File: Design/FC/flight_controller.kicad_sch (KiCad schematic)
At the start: 3 parts, among them U1 STM32H747BIT6

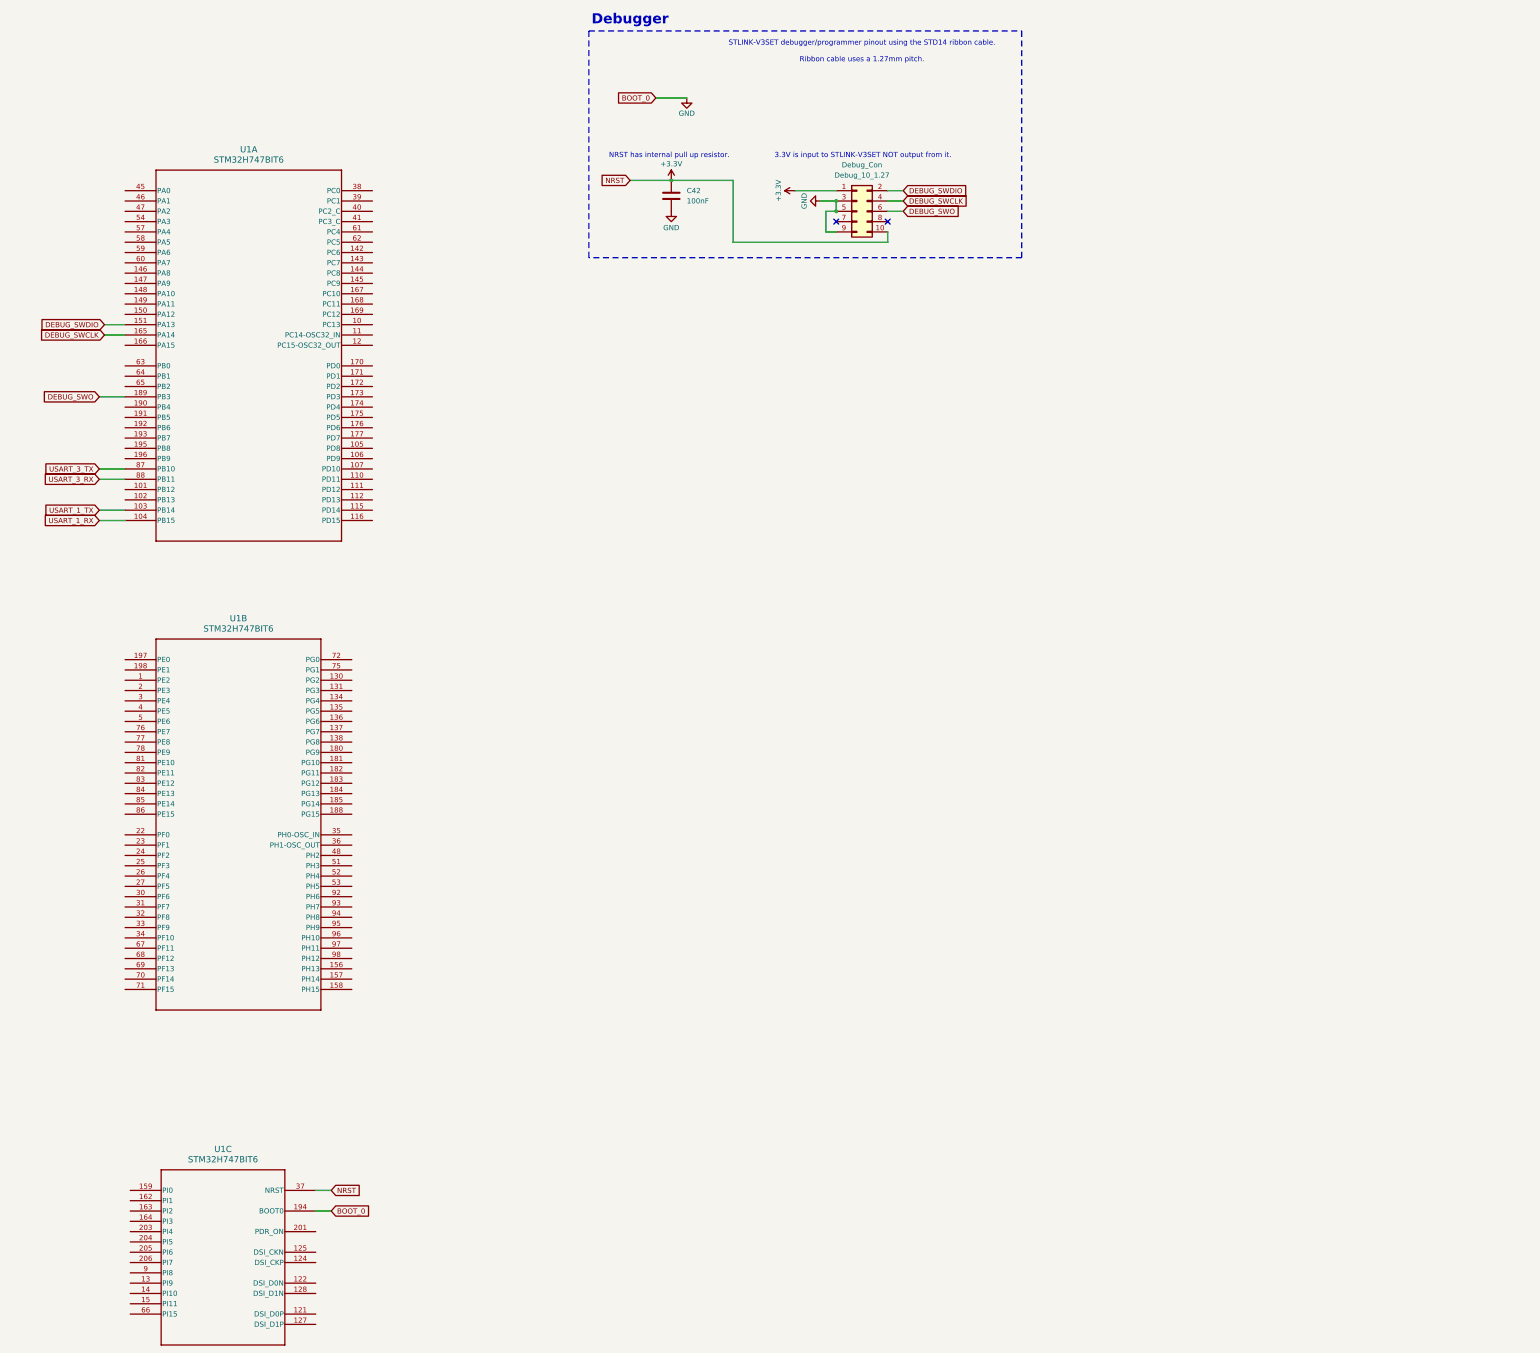
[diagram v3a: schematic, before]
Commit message: started adding periphs
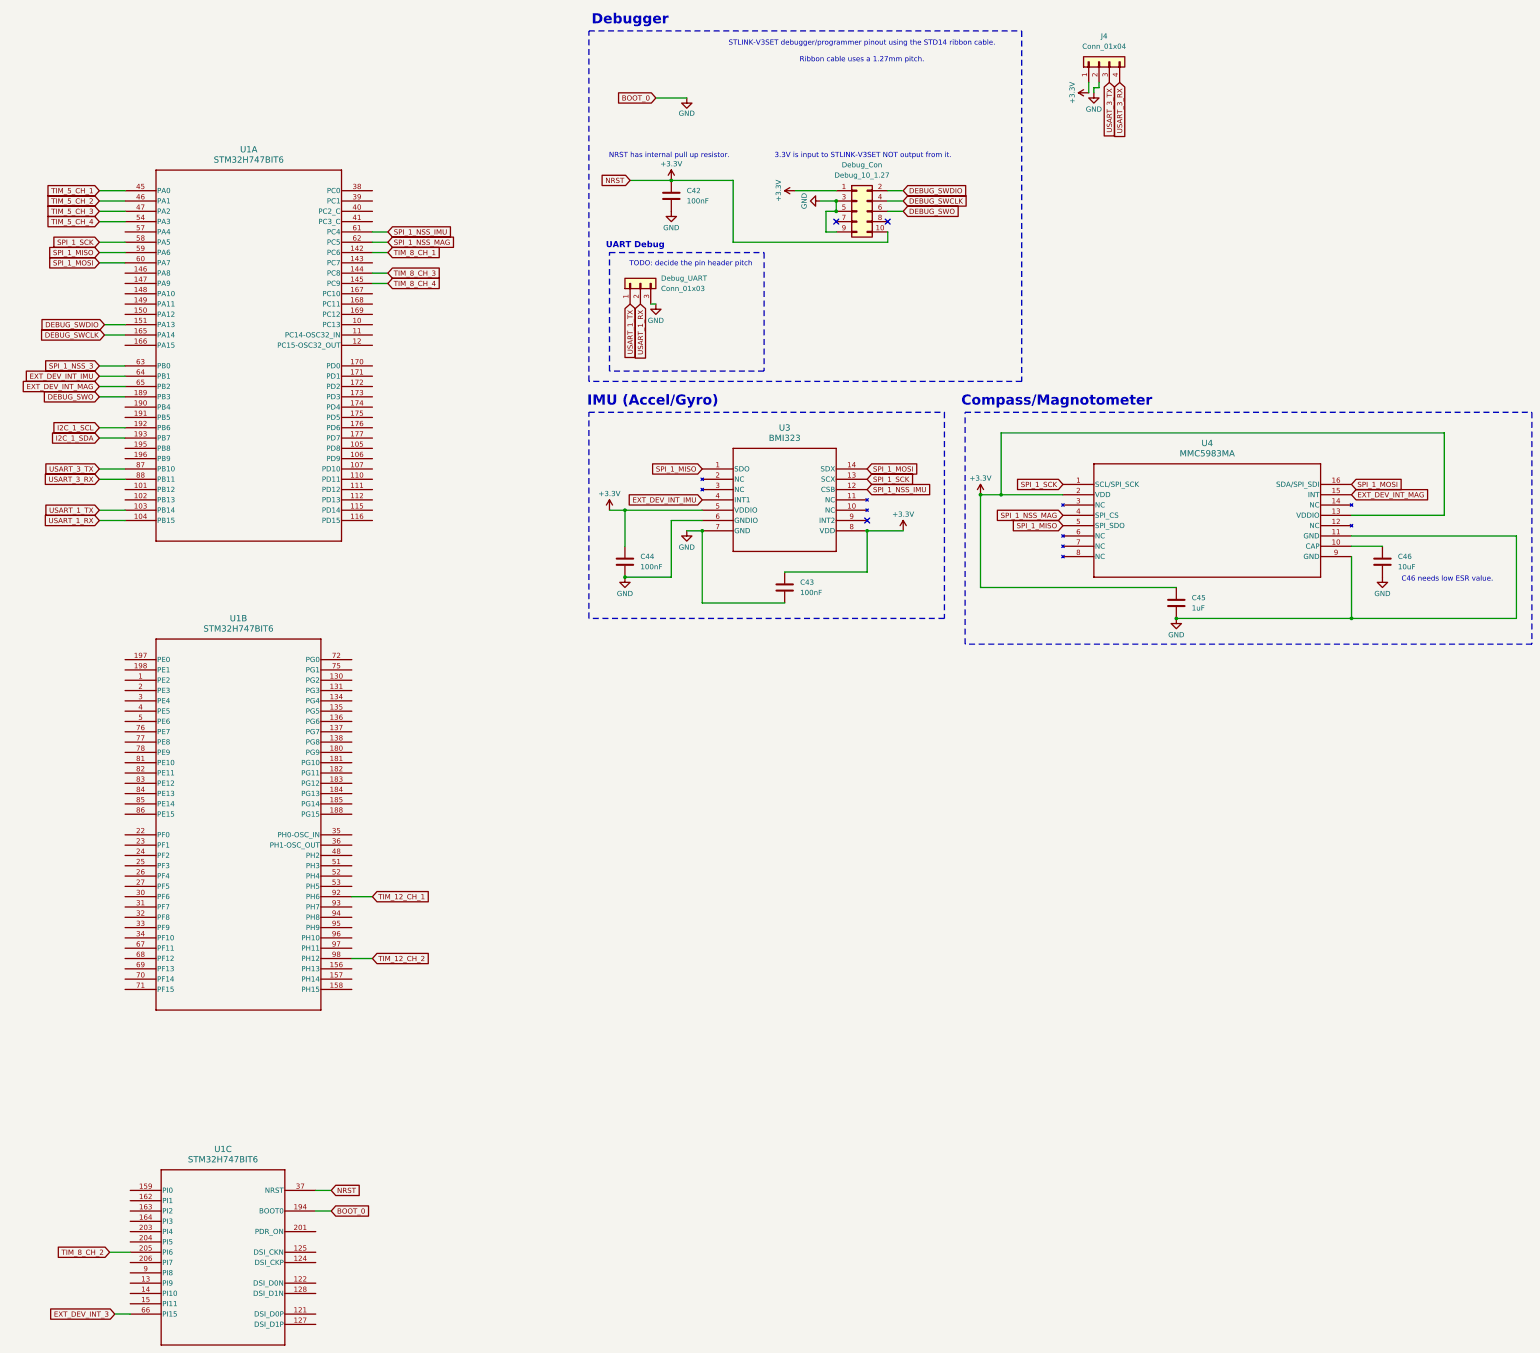
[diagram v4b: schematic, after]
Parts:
- added C43, C44: 100nF, symbol Device:C
- added C45: 1uF, symbol Device:C
- added C46: 10uF, symbol Device:C
- added Debug_UART: Conn_01x03, symbol Connector_Generic:Conn_01x03
- added J4: Conn_01x04, symbol Connector_Generic:Conn_01x04
- added U3: BMI323, BMI323_BOS, symbol BMI323:BMI323
- added U4: MMC5983MA, MMC5983MA_MEM, symbol MMC5983MA:MMC5983MA
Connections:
- net +3.3V: now also C43.1, C44.1, C45.1, J4.1 (Pin_1), U3.5 (VDDIO), U3.8 (VDD), U4.13 (VDDIO), U4.2 (VDD)
- net GND: now also C43.2, C44.2, C45.2, C46.2, Debug_UART.3 (Pin_3), J4.2 (Pin_2), U3.6 (GNDIO), U3.7 (GND), U4.11 (GND), U4.9 (GND)
- net USART_1_RX: now also Debug_UART.2 (Pin_2)
- net USART_1_TX: now also Debug_UART.1 (Pin_1)
- net USART_3_RX: now also J4.4 (Pin_4)
- net USART_3_TX: now also J4.3 (Pin_3)
- net TIM_8_CH_1: now reaches U1.142 (PC6)
- net TIM_8_CH_3: now reaches U1.144 (PC8)
- net TIM_8_CH_4: now reaches U1.145 (PC9)
- net I2C_1_SCL: now reaches U1.192 (PB6)
- net I2C_1_SDA: now reaches U1.193 (PB7)
- net TIM_5_CH_1: now reaches U1.45 (PA0)
- net TIM_5_CH_2: now reaches U1.46 (PA1)
- net TIM_5_CH_3: now reaches U1.47 (PA2)
- net TIM_5_CH_4: now reaches U1.54 (PA3)
- net SPI_1_SCK: now reaches U1.58 (PA5)
- net SPI_1_SCK: now also U3.13 (SCX), U4.1 (SCL/SPI_SCK)
- net SPI_1_MISO: now reaches U1.59 (PA6)
- net SPI_1_MISO: now also U3.1 (SDO), U4.5 (SPI_SDO)
- net SPI_1_MOSI: now reaches U1.60 (PA7)
- net SPI_1_MOSI: now also U3.14 (SDX), U4.16 (SDA/SPI_SDI)
- net SPI_1_NSS_IMU: now reaches U1.61 (PC4)
- net SPI_1_NSS_IMU: now also U3.12 (CSB)
- net SPI_1_NSS_MAG: now reaches U1.62 (PC5)
- net SPI_1_NSS_MAG: now also U4.4 (SPI_CS)
- net SPI_1_NSS_3: now reaches U1.63 (PB0)
- net EXT_DEV_INT_IMU: now reaches U1.64 (PB1)
- net EXT_DEV_INT_IMU: now also U3.4 (INT1)
- net EXT_DEV_INT_MAG: now reaches U1.65 (PB2)
- net EXT_DEV_INT_MAG: now also U4.15 (INT)
- net TIM_8_CH_2: now reaches U1.205 (PI6)
- net EXT_DEV_INT_3: now reaches U1.66 (PI15)
- net TIM_12_CH_1: now reaches U1.92 (PH6)
- net TIM_12_CH_2: now reaches U1.98 (PH12)
- new net: C46.1, U4.10 (CAP)
- no-connect marks 2 -> 3
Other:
- note added: "C46 needs low ESR value."
- note added: "Compass/Magnotometer"
- note added: "IMU (Accel/Gyro)"
- note added: "TODO: decide the pin header pitch"
- note added: "UART Debug"

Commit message: continuing to add periphs
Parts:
- added C47, C48: 100nF, symbol Device:C
- added JL_Servo_2, L_Servo_1, L_Servo_3, L_Servo_4, R_Servo_1, R_Servo_2, R_Servo_3, R_Servo_4: Conn_01x03, symbol Connector_Generic:Conn_01x03
- added L_Motor, R_Motor: Conn_01x02, symbol Connector_Generic:Conn_01x02
- added U5: BMP390, BMP390-10LGA_2X2X0p75_BOS, symbol BMP390:BMP390
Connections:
- net +3.3V: now also C47.1, C48.1, U5.1 (VDDIO), U5.10 (VDD)
- net GND: now also C47.2, C48.2, JL_Servo_2.1 (Pin_1), L_Motor.1 (Pin_1), L_Servo_1.1 (Pin_1), L_Servo_3.1 (Pin_1), L_Servo_4.1 (Pin_1), R_Motor.1 (Pin_1), R_Servo_1.1 (Pin_1), R_Servo_2.1 (Pin_1), R_Servo_3.1 (Pin_1), R_Servo_4.1 (Pin_1), U5.3 (VSS), U5.8 (VSS), U5.9 (VSS)
- net SPI_1_MISO: now also U5.5 (SDO)
- net SPI_1_MOSI: now also U5.4 (SDI)
- net SPI_1_SCK: now also U5.2 (SCK)
- net TIM_5_CH_1: now also L_Servo_1.3 (Pin_3)
- net TIM_5_CH_2: now also JL_Servo_2.3 (Pin_3)
- net TIM_5_CH_3: now also L_Servo_3.3 (Pin_3)
- net TIM_5_CH_4: now also L_Servo_4.3 (Pin_3)
- net TIM_8_CH_1: now also R_Servo_1.3 (Pin_3)
- net TIM_8_CH_2: now also R_Servo_2.3 (Pin_3)
- net TIM_8_CH_3: now also R_Servo_3.3 (Pin_3)
- net TIM_8_CH_4: now also R_Servo_4.3 (Pin_3)
- net TIM_4_CH_1: now reaches U1.111 (PD12)
- net TIM_4_CH_1: now also R_Motor.2 (Pin_2)
- net TIM_16_CH_1: now reaches U1.30 (PF6)
- net TIM_16_CH_1: now also L_Motor.2 (Pin_2)
- net EXT_DEV_INT_3 renamed EXT_DEV_INT_BARO
- net EXT_DEV_INT_BARO: now also U5.7 (INT)
- net SPI_1_NSS_3 renamed SPI_1_NSS_BARO
- net SPI_1_NSS_BARO: now also U5.6 (CSB)
- new net +5V: JL_Servo_2.2 (Pin_2), L_Servo_1.2 (Pin_2), L_Servo_3.2 (Pin_2), L_Servo_4.2 (Pin_2), R_Servo_1.2 (Pin_2), R_Servo_2.2 (Pin_2), R_Servo_3.2 (Pin_2), R_Servo_4.2 (Pin_2)
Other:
- note added: "Barometer"
- note added: "Servo (GND, VCC, Signal) and Motor (GND, Signal) Connectors"

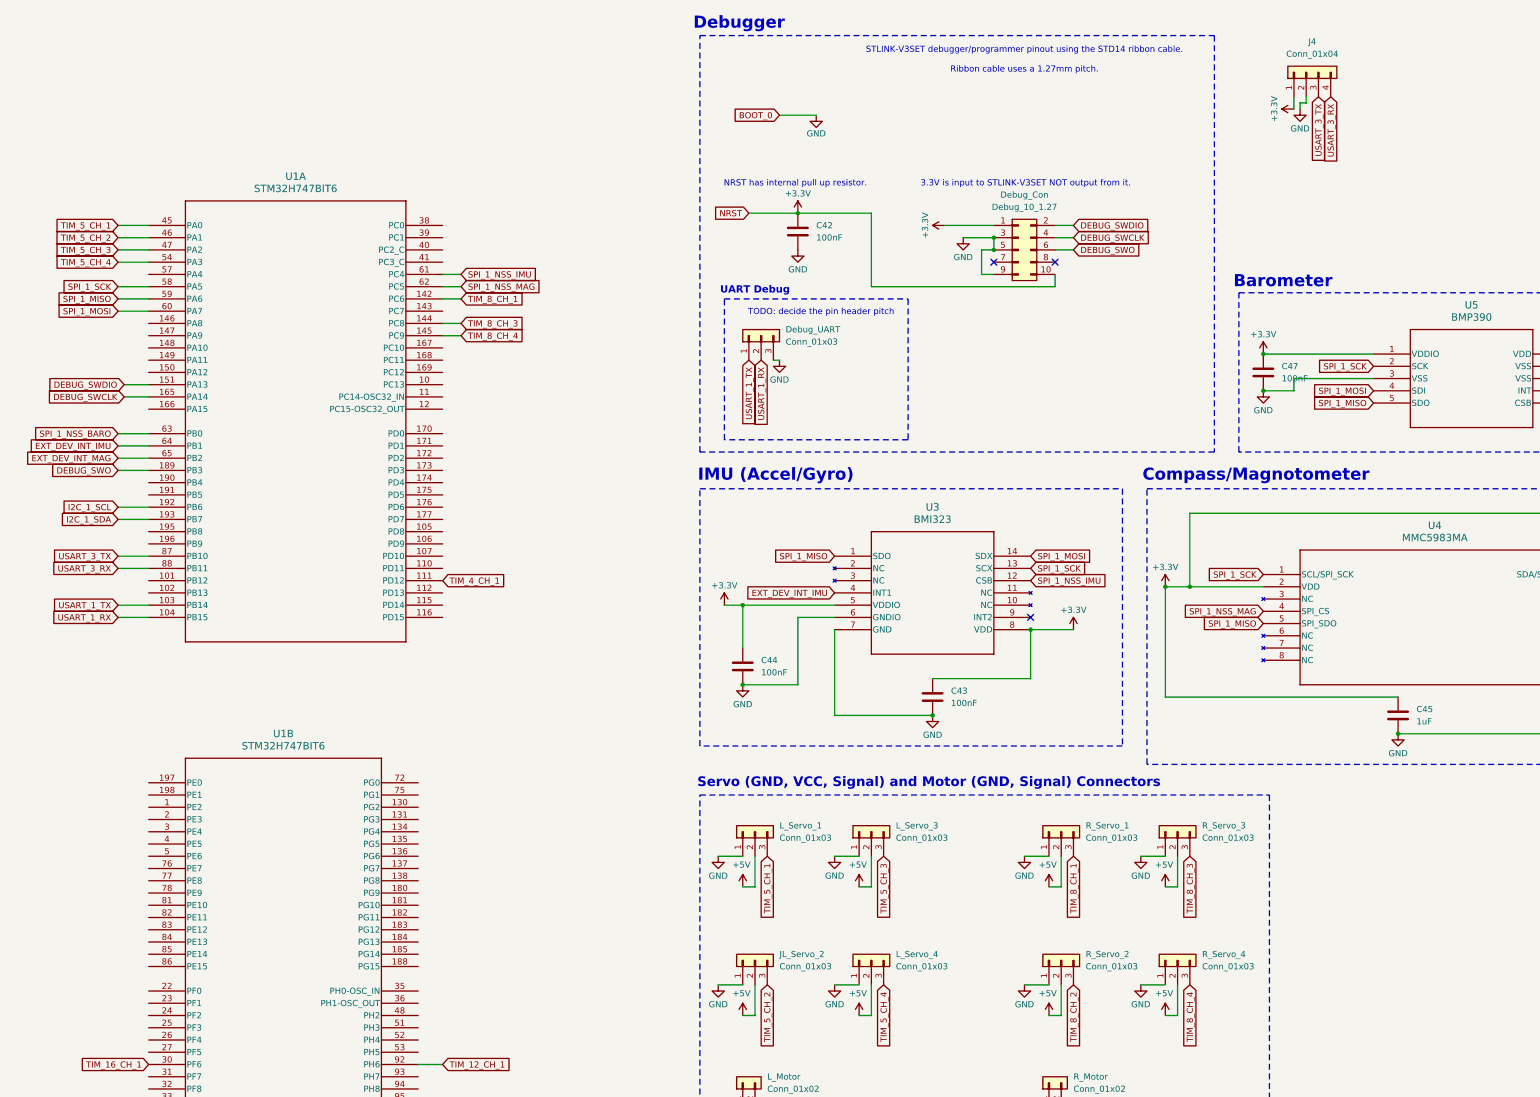
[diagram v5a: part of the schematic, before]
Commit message: added pull up resistors
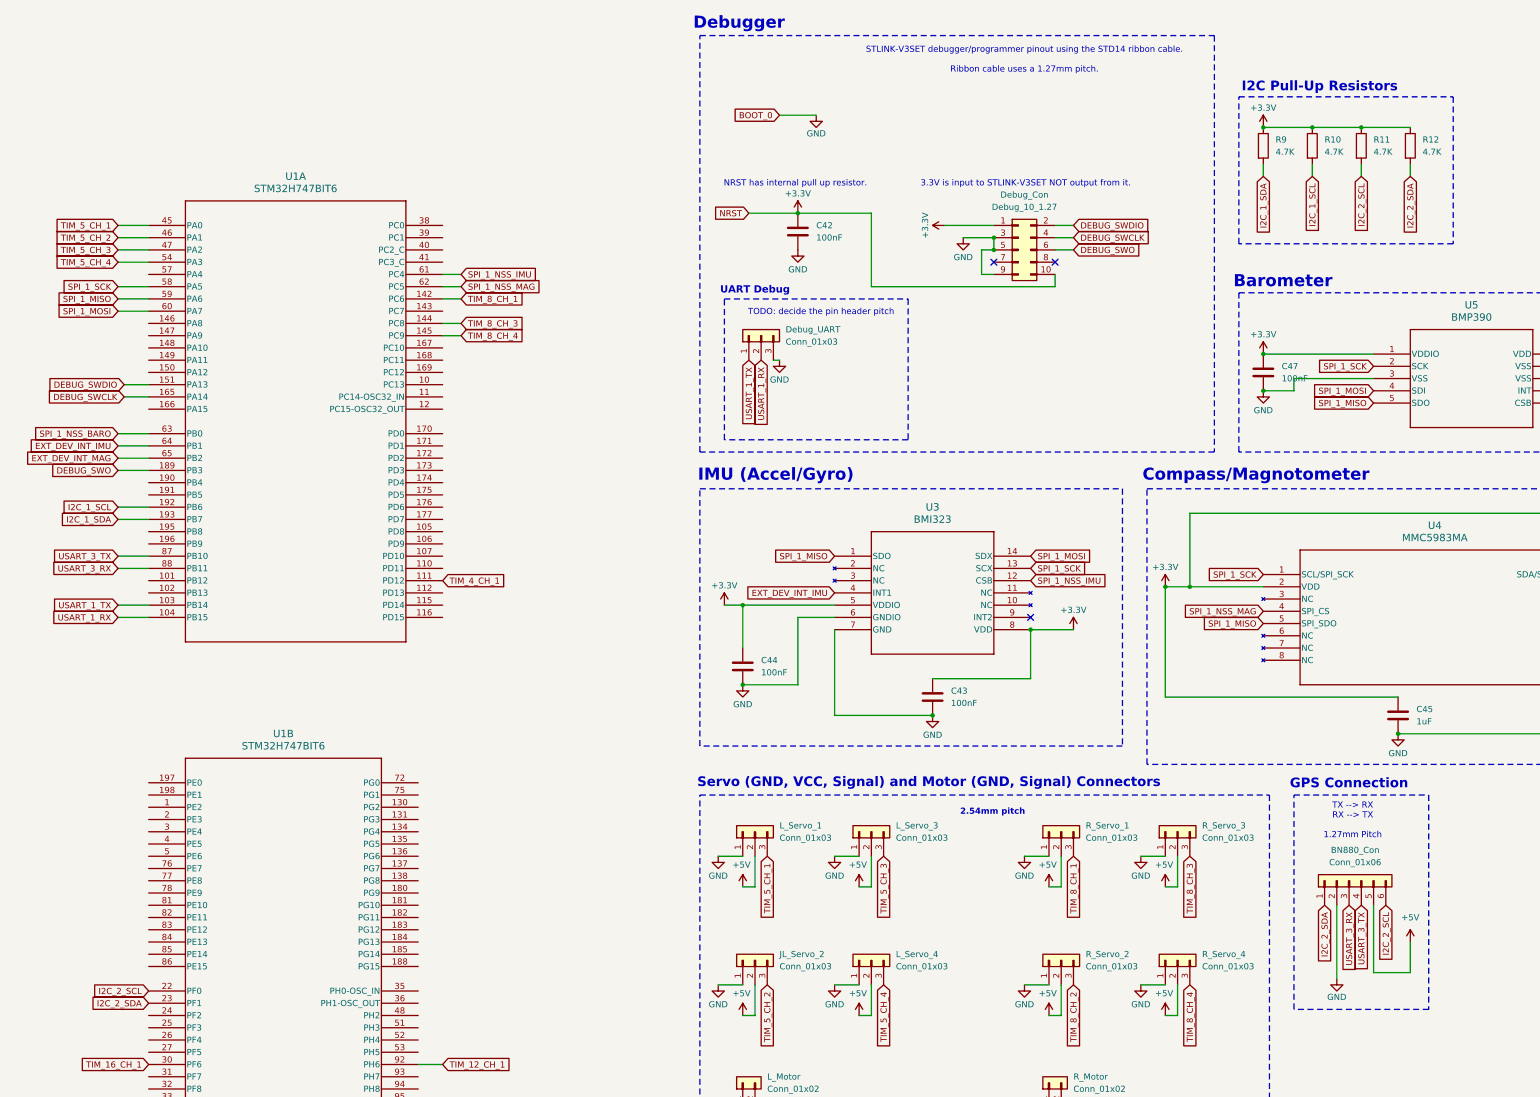
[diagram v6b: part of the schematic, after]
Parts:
- removed J4: Conn_01x04, symbol Connector_Generic:Conn_01x04
- added BN880_Con: Conn_01x06, symbol Connector_Generic:Conn_01x06
- added R10, R11, R12, R9: 4.7K, symbol Device:R
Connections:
- net +3.3V: now also R10.1, R11.1, R12.1, R9.1
- net +5V: now also BN880_Con.5 (Pin_5)
- net GND: now also BN880_Con.2 (Pin_2)
- net I2C_1_SCL: now also R10.2
- net I2C_1_SDA: now also R9.2
- net USART_3_RX: now also BN880_Con.3 (Pin_3)
- net USART_3_TX: now also BN880_Con.4 (Pin_4)
- net I2C_2_SCL: now reaches U1.22 (PF0)
- net I2C_2_SCL: now also BN880_Con.6 (Pin_6), R11.2
- net I2C_2_SDA: now reaches U1.23 (PF1)
- net I2C_2_SDA: now also BN880_Con.1 (Pin_1), R12.2
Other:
- note added: "2.54mm pitch"
- note added: "GPS Connection"
- note added: "I2C Pull-Up Resistors"
- note added: "TX --> RX RX --> TX 1.27mm Pitch"
